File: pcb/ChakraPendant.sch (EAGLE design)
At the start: 19 parts, among them Q1 MOSFET-NCHANNEL2N7002PW

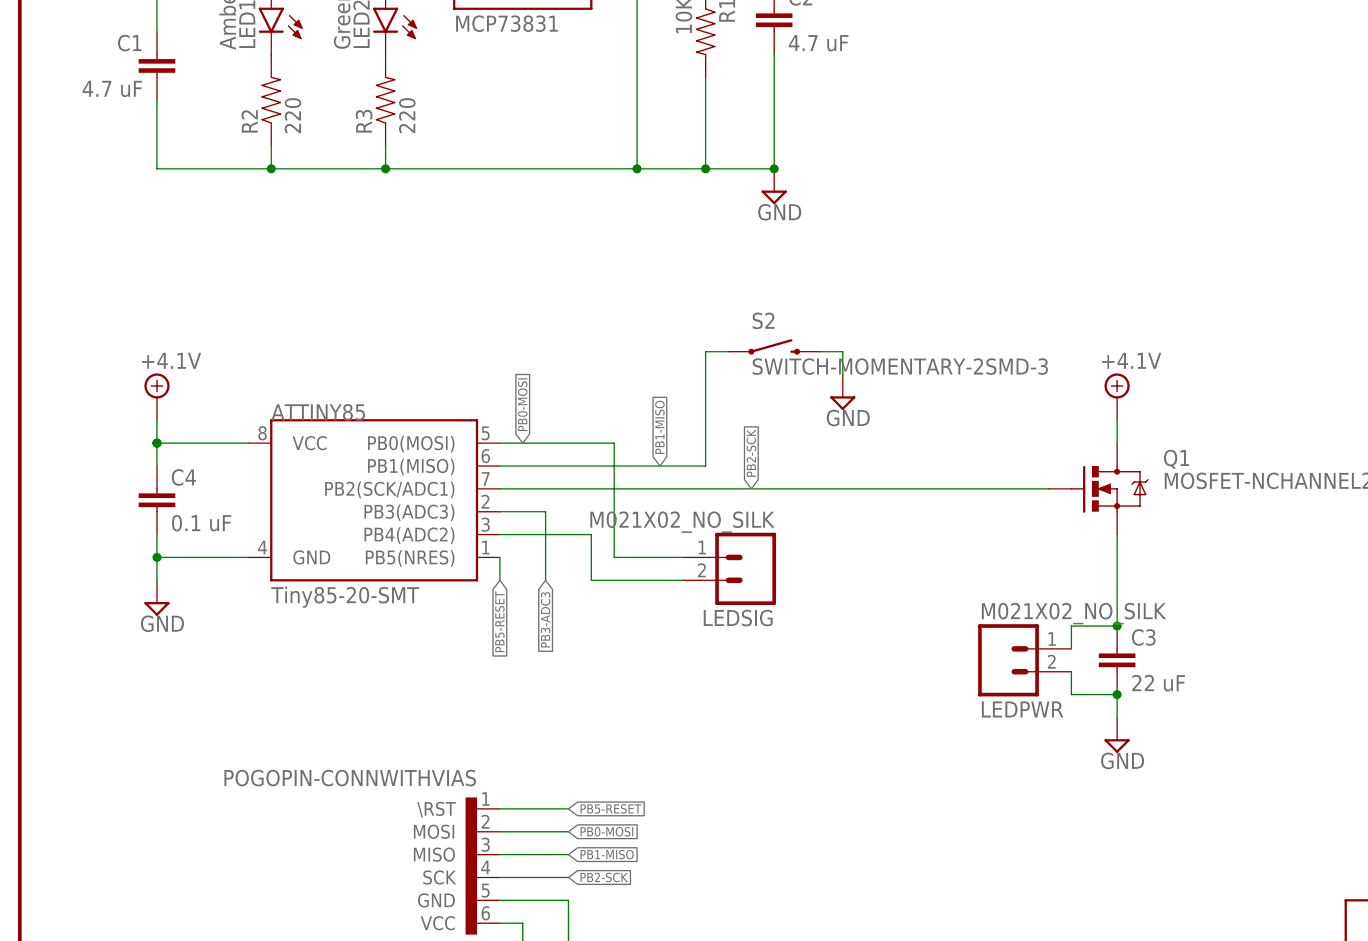
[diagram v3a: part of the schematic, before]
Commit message: Swap clock and data. Oops.
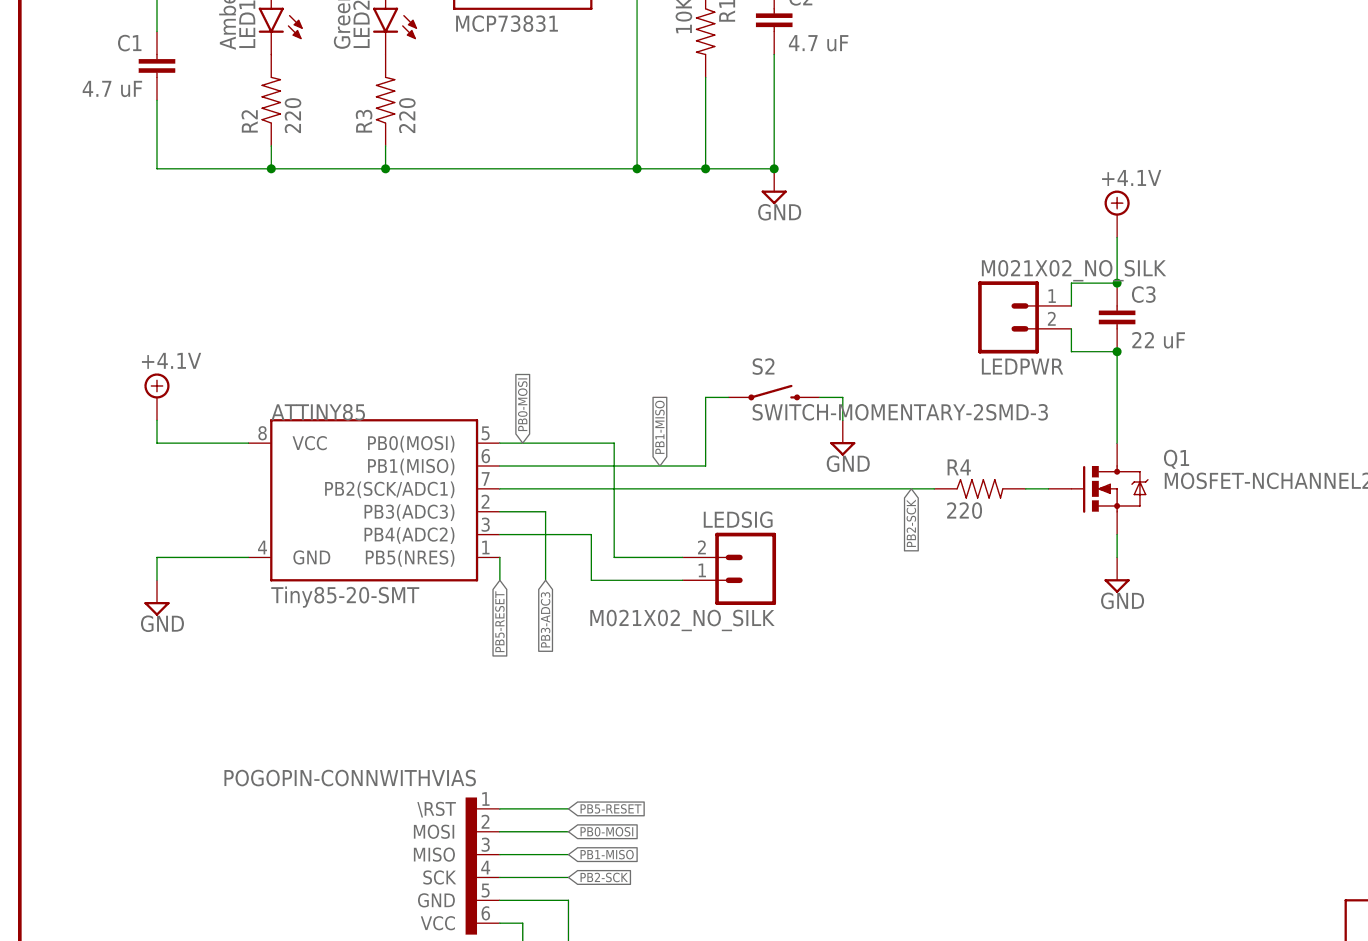
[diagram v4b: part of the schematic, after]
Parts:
- removed C4: 0.1 uF, SparkFun-Passives:CAP0603-CAP
- added R4: 220, SparkFun-Passives:RESISTOR0603-RES
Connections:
- new net N$2: C3.2, LEDPWR.2, Q1.D
- net +4.1V: now also C3.1, LEDPWR.1; no longer C4.1, Q1.D
- net GND: now also Q1.S; no longer C3.2, C4.2, LEDPWR.2
- net N$1: now also Q1.G, R4.2; no longer C3.1, LEDPWR.1, Q1.S
- net N$3: now also LEDSIG.1; no longer LEDSIG.2
- net PB0-MOSI: now also LEDSIG.2; no longer LEDSIG.1
- net PB2-SCK: now also R4.1; no longer Q1.G
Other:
- moved on the sheet: C3, LEDPWR, LEDSIG, S2
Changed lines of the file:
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@@
 <part name="U$1" library="Protofusion" deviceset="POGOPIN-CONN" device="WITHVIAS"/>
 <part name="S2" library="SparkFun-Electromechanical" deviceset="SWITCH-MOMENTARY-2" device="SMD-3"/>
-<part name="C4" library="SparkFun-Passives" deviceset="CAP" device="0603-CAP" value="0.1 uF"/>
 <part name="LEDPWR" library="SparkFun-Connectors" deviceset="M02" device="1X02_NO_SILK"/>
 <part name="LEDSIG" library="SparkFun-Connectors" deviceset="M02" device="1X02_NO_SILK"/>
@@
 <part name="SUPPLY1" library="supply2" deviceset="GND" device=""/>
 <part name="FRAME1" library="SparkFun-Aesthetics" deviceset="FRAME-LETTER" device=""/>
+<part name="R4" library="SparkFun-Passives" deviceset="RESISTOR" device="0603-RES" value="220"/>
 </parts>
 <sheets>
@@
 <instance part="JP1" gate="G$1" x="12.7" y="154.94" rot="MR90"/>
 <instance part="SUPPLY2" gate="GND" x="15.24" y="68.58"/>
-<instance part="SUPPLY5" gate="GND" x="121.92" y="53.34"/>
-<instance part="SUPPLY6" gate="GND" x="91.44" y="91.44"/>
+<instance part="SUPPLY5" gate="GND" x="121.92" y="71.12"/>
+<instance part="SUPPLY6" gate="GND" x="91.44" y="86.36"/>
 <instance part="SUPPLY9" gate="GND" x="60.96" y="27.94"/>
 <instance part="CHARGE" gate="G$1" x="55.88" y="139.7"/>
@@
 <instance part="C1" gate="G$1" x="15.24" y="127" rot="MR0"/>
 <instance part="C2" gate="G$1" x="83.82" y="132.08"/>
-<instance part="C3" gate="G$1" x="121.92" y="60.96"/>
+<instance part="C3" gate="G$1" x="121.92" y="99.06"/>
 <instance part="Q1" gate="G$1" x="121.92" y="81.28"/>
 <instance part="U$1" gate="J" x="50.8" y="38.1" rot="R180"/>
-<instance part="S2" gate="G$1" x="83.82" y="96.52"/>
-<instance part="C4" gate="G$1" x="15.24" y="78.74"/>
-<instance part="LEDPWR" gate="G$1" x="109.22" y="63.5" rot="MR180"/>
-<instance part="LEDSIG" gate="G$1" x="81.28" y="73.66" rot="R180"/>
+<instance part="S2" gate="G$1" x="83.82" y="91.44"/>
+<instance part="LEDPWR" gate="G$1" x="109.22" y="101.6" rot="MR180"/>
+<instance part="LEDSIG" gate="G$1" x="81.28" y="71.12" rot="MR0"/>
 <instance part="LED1" gate="G$1" x="27.94" y="134.62" rot="MR0"/>
 <instance part="LED2" gate="G$1" x="40.64" y="134.62" rot="MR0"/>
@@
 <instance part="R3" gate="G$1" x="40.64" y="124.46" rot="R90"/>
 <instance part="SUPPLY7" gate="P" x="55.88" y="27.94" rot="R180"/>
-<instance part="SUPPLY11" gate="P" x="121.92" y="91.44"/>
+<instance part="SUPPLY11" gate="P" x="121.92" y="111.76"/>
 <instance part="SUPPLY12" gate="P" x="15.24" y="91.44"/>
 <instance part="SUPPLY13" gate="P" x="83.82" y="147.32"/>
@@
 <instance part="FRAME1" gate="G$1" x="0" y="0"/>
 <instance part="FRAME1" gate="G$2" x="147.32" y="0"/>
+<instance part="R4" gate="G$1" x="106.68" y="81.28"/>
 </instances>
 <busses>
@@
 <wire x1="15.24" y1="73.66" x2="15.24" y2="71.12" width="0.1524" layer="91"/>
 <pinref part="SUPPLY2" gate="GND" pin="GND"/>
-<pinref part="C4" gate="G$1" pin="2"/>
-<wire x1="15.24" y1="73.66" x2="15.24" y2="76.2" width="0.1524" layer="91"/>
-<junction x="15.24" y="73.66"/>
-</segment>
-<segment>
-<pinref part="SUPPLY5" gate="GND" pin="GND"/>
-<pinref part="C3" gate="G$1" pin="2"/>
-<pinref part="LEDPWR" gate="G$1" pin="2"/>
-<wire x1="121.92" y1="55.88" x2="121.92" y2="58.42" width="0.1524" layer="91"/>
-<junction x="121.92" y="58.42"/>
-<wire x1="116.84" y1="60.96" x2="116.84" y2="58.42" width="0.1524" layer="91"/>
-<wire x1="116.84" y1="58.42" x2="121.92" y2="58.42" width="0.1524" layer="91"/>
 </segment>
 <segment>
@@
 <pinref part="SUPPLY6" gate="GND" pin="GND"/>
 <pinref part="S2" gate="G$1" pin="2"/>
-<wire x1="88.9" y1="96.52" x2="91.44" y2="96.52" width="0.1524" layer="91"/>
-<wire x1="91.44" y1="96.52" x2="91.44" y2="93.98" width="0.1524" layer="91"/>
+<wire x1="88.9" y1="91.44" x2="91.44" y2="91.44" width="0.1524" layer="91"/>
+<wire x1="91.44" y1="91.44" x2="91.44" y2="88.9" width="0.1524" layer="91"/>
 </segment>
 <segment>
@@
 <pinref part="SUPPLY1" gate="GND" pin="GND"/>
 </segment>
+<segment>
+<pinref part="SUPPLY5" gate="GND" pin="GND"/>
+<pinref part="Q1" gate="G$1" pin="S"/>
+<wire x1="121.92" y1="73.66" x2="121.92" y2="76.2" width="0.1524" layer="91"/>
+</segment>
 </net>
 <net name="PB0-MOSI" class="0">
@@
 </segment>
 <segment>
-<pinref part="LEDSIG" gate="G$1" pin="1"/>
 <pinref part="ATTINY85" gate="G$1" pin="PB0(MOSI)"/>
-<wire x1="66.04" y1="73.66" x2="73.66" y2="73.66" width="0.1524" layer="91"/>
 <label x="55.88" y="86.36" size="1.016" layer="95" rot="R90" xref="yes"/>
 <wire x1="53.34" y1="86.36" x2="66.04" y2="86.36" width="0.1524" layer="91"/>
 <wire x1="66.04" y1="86.36" x2="66.04" y2="73.66" width="0.1524" layer="91"/>
+<pinref part="LEDSIG" gate="G$1" pin="2"/>
+<wire x1="73.66" y1="73.66" x2="66.04" y2="73.66" width="0.1524" layer="91"/>
 </segment>
 </net>
@@
 <label x="71.12" y="83.82" size="1.016" layer="95" rot="R90" xref="yes"/>
 <pinref part="S2" gate="G$1" pin="1"/>
-<wire x1="76.2" y1="83.82" x2="76.2" y2="96.52" width="0.1524" layer="91"/>
-<wire x1="78.74" y1="96.52" x2="76.2" y2="96.52" width="0.1524" layer="91"/>
+<wire x1="76.2" y1="83.82" x2="76.2" y2="91.44" width="0.1524" layer="91"/>
+<wire x1="78.74" y1="91.44" x2="76.2" y2="91.44" width="0.1524" layer="91"/>
 <wire x1="53.34" y1="83.82" x2="76.2" y2="83.82" width="0.1524" layer="91"/>
 </segment>
@@
 <net name="PB2-SCK" class="0">
 <segment>
-<pinref part="Q1" gate="G$1" pin="G"/>
-<pinref part="ATTINY85" gate="G$1" pin="PB2(SCK/ADC1)"/>
-<label x="81.28" y="81.28" size="1.016" layer="95" rot="R90" xref="yes"/>
-<wire x1="114.3" y1="81.28" x2="53.34" y2="81.28" width="0.1524" layer="91"/>
-</segment>
-<segment>
 <pinref part="U$1" gate="J" pin="SCK"/>
 <wire x1="53.34" y1="38.1" x2="60.96" y2="38.1" width="0.1524" layer="91"/>
 <label x="60.96" y="38.1" size="1.016" layer="95" xref="yes"/>
+<label x="99.06" y="81.28" size="1.016" layer="95" rot="R270" xref="yes"/>
+</segment>
+<segment>
+<pinref part="ATTINY85" gate="G$1" pin="PB2(SCK/ADC1)"/>
+<wire x1="53.34" y1="81.28" x2="101.6" y2="81.28" width="0.1524" layer="91"/>
+<pinref part="R4" gate="G$1" pin="1"/>
 </segment>
 </net>
@@
 <wire x1="66.04" y1="139.7" x2="76.2" y2="139.7" width="0.1524" layer="91"/>
 <wire x1="76.2" y1="139.7" x2="76.2" y2="137.16" width="0.1524" layer="91"/>
-</segment>
-</net>
-<net name="N$1" class="1">
-<segment>
-<pinref part="C3" gate="G$1" pin="1"/>
-<pinref part="LEDPWR" gate="G$1" pin="1"/>
-<wire x1="116.84" y1="63.5" x2="116.84" y2="66.04" width="0.1524" layer="91"/>
-<wire x1="116.84" y1="66.04" x2="121.92" y2="66.04" width="0.1524" layer="91"/>
-<pinref part="Q1" gate="G$1" pin="S"/>
-<wire x1="121.92" y1="76.2" x2="121.92" y2="66.04" width="0.1524" layer="91"/>
-<junction x="121.92" y="66.04"/>
 </segment>
 </net>
@@
 <pinref part="ATTINY85" gate="G$1" pin="PB4(ADC2)"/>
 <wire x1="53.34" y1="76.2" x2="63.5" y2="76.2" width="0.1524" layer="91"/>
-<pinref part="LEDSIG" gate="G$1" pin="2"/>
 <wire x1="63.5" y1="76.2" x2="63.5" y2="71.12" width="0.1524" layer="91"/>
+<pinref part="LEDSIG" gate="G$1" pin="1"/>
 <wire x1="63.5" y1="71.12" x2="73.66" y2="71.12" width="0.1524" layer="91"/>
 </segment>
@@
 <pinref part="ATTINY85" gate="G$1" pin="VCC"/>
 <wire x1="15.24" y1="86.36" x2="25.4" y2="86.36" width="0.1524" layer="91"/>
-<junction x="15.24" y="86.36"/>
-<junction x="15.24" y="86.36"/>
 <pinref part="SUPPLY12" gate="P" pin="+4.1V"/>
 <wire x1="15.24" y1="88.9" x2="15.24" y2="86.36" width="0.1524" layer="91"/>
-<pinref part="C4" gate="G$1" pin="1"/>
-<wire x1="15.24" y1="83.82" x2="15.24" y2="86.36" width="0.1524" layer="91"/>
-</segment>
-<segment>
+</segment>
+<segment>
+<pinref part="C3" gate="G$1" pin="1"/>
+<pinref part="LEDPWR" gate="G$1" pin="1"/>
+<wire x1="116.84" y1="101.6" x2="116.84" y2="104.14" width="0.1524" layer="91"/>
+<wire x1="116.84" y1="104.14" x2="121.92" y2="104.14" width="0.1524" layer="91"/>
+<pinref part="SUPPLY11" gate="P" pin="+4.1V"/>
+<wire x1="121.92" y1="109.22" x2="121.92" y2="104.14" width="0.1524" layer="91"/>
+<junction x="121.92" y="104.14"/>
+</segment>
+</net>
+<net name="N$2" class="1">
+<segment>
+<pinref part="C3" gate="G$1" pin="2"/>
+<pinref part="LEDPWR" gate="G$1" pin="2"/>
+<wire x1="116.84" y1="99.06" x2="116.84" y2="96.52" width="0.1524" layer="91"/>
+<wire x1="116.84" y1="96.52" x2="121.92" y2="96.52" width="0.1524" layer="91"/>
 <pinref part="Q1" gate="G$1" pin="D"/>
-<pinref part="SUPPLY11" gate="P" pin="+4.1V"/>
-<wire x1="121.92" y1="86.36" x2="121.92" y2="88.9" width="0.1524" layer="91"/>
-</segment>
-</net>
+<wire x1="121.92" y1="96.52" x2="121.92" y2="86.36" width="0.1524" layer="91"/>
+<junction x="121.92" y="96.52"/>
+</segment>
+</net>
+<net name="N$1" class="0">
+<segment>
+<pinref part="R4" gate="G$1" pin="2"/>
+<pinref part="Q1" gate="G$1" pin="G"/>
+<wire x1="111.76" y1="81.28" x2="114.3" y2="81.28" width="0.1524" layer="91"/>
+</segment>
+</net>
